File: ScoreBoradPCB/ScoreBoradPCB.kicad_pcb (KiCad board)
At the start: 2 copper layers, 100 x 100 mm, 129 parts, among them J1 Conn_01x08_Male, J10 Conn_01x02_Male, J2 Conn_01x08_Male, J3 Conn_01x08_Male, J4 Conn_01x04_Male, J5 Conn_01x04_Male, J6 Conn_01x02_Male, J7 Conn_01x02_Male, J8 Conn_01x06_Male, J9 Conn_01x02_Male, Q1 2N7002K, Q10 NP52N06SLG, Q11 2N7002K, Q12 NP52N06SLG, Q13 2N7002K, Q14 NP52N06SLG, Q15 BSS84, Q16 NP52N06SLG, Q17 2N7002K, Q18 BSS84, Q19 NP52N06SLG, Q2 NP52N06SLG, Q20 2N7002K, Q21 BSS84, Q22 NP52N06SLG, Q23 2N7002K, Q24 2N7002K, Q3 2N7002K, Q4 NP52N06SLG, Q5 2N7002K, Q6 NP52N06SLG, Q7 2N7002K, Q8 NP52N06SLG, Q9 2N7002K, SW1 SW_Push, SW2 SW_Push, SW3 SW_Push, SW4 SW_Push, SW5 SW_Push, SW6 SW_Push, SW7 SW_Push, U1 PIC16F1938, U2 TLP291, U3 IR2104, U4 TLP291, U5 IR2104, U6 TLP291, U7 IR2104

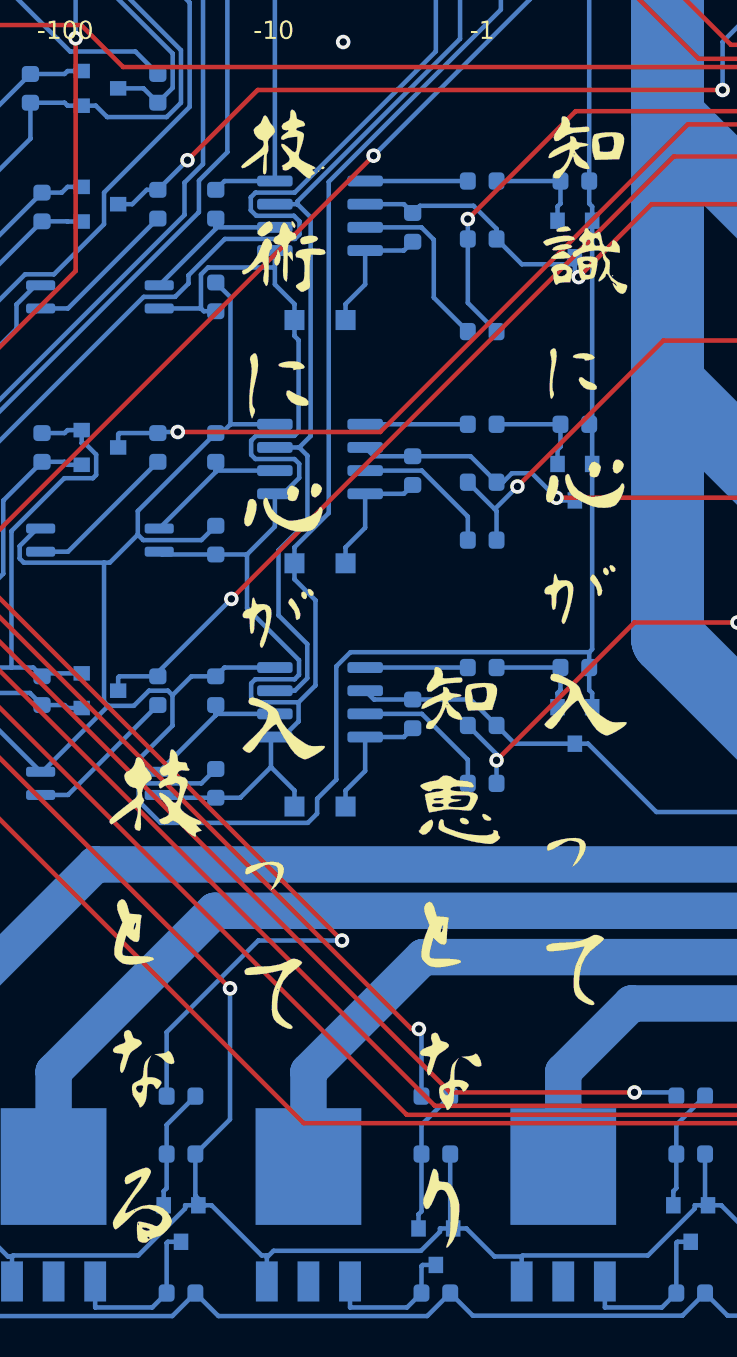
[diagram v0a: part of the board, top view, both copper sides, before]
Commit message: ゲート抵抗を削除
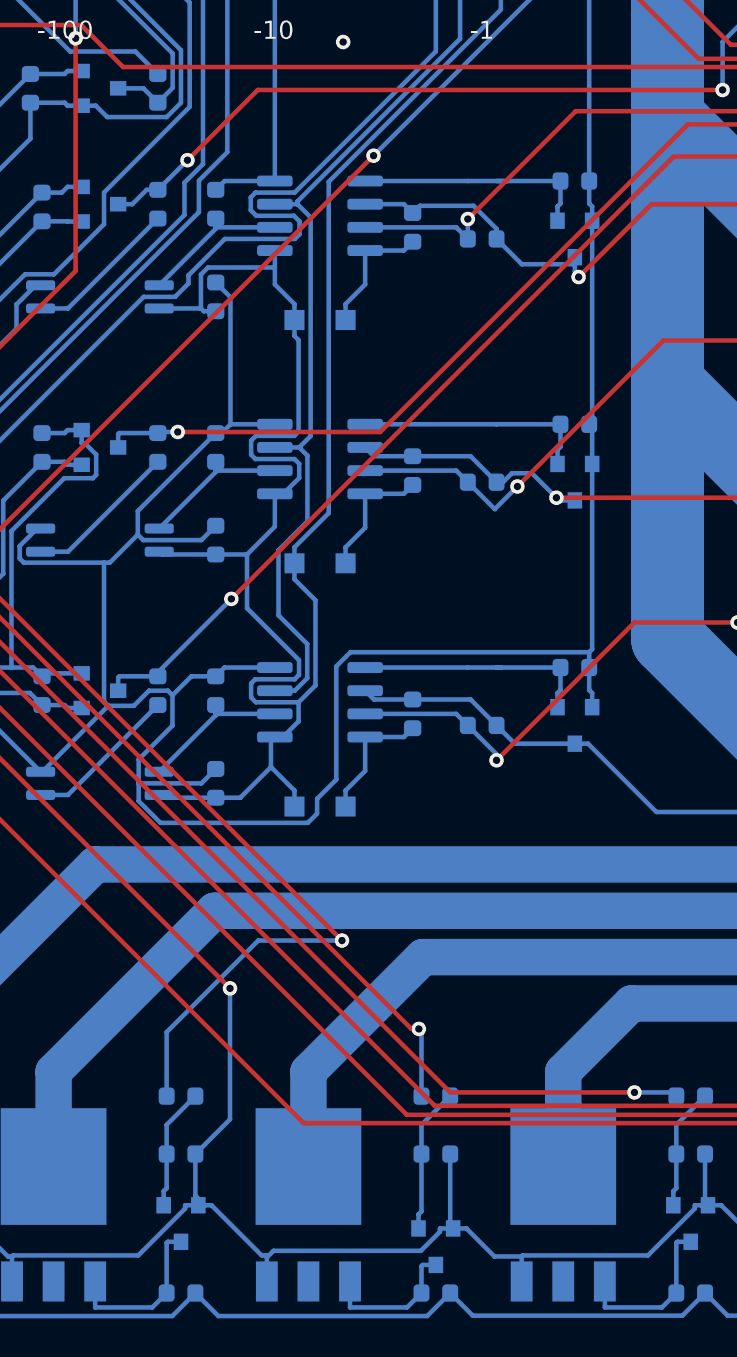
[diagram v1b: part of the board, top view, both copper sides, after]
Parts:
- removed G***: LOGO, logo:Koukun
- removed R25, R26, R32, R33, R39, R40: 100, Resistor_SMD:R_0603_1608Metric
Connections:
- U3 pad 5: Net-(R26-Pad2) -> Net-(Q17-Pad1)
- U3 pad 7: Net-(R25-Pad2) -> Net-(Q16-Pad1)
- U5 pad 5: Net-(R33-Pad2) -> Net-(Q20-Pad1)
- U5 pad 7: Net-(R32-Pad2) -> Net-(Q19-Pad1)
- U7 pad 5: Net-(R40-Pad2) -> Net-(Q23-Pad1)
- U7 pad 7: Net-(R39-Pad2) -> Net-(Q22-Pad1)
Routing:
- net Net-(R25-Pad2): track 9.85 -> 0.00 mm
- net Net-(R32-Pad2): track 7.96 -> 0.00 mm
- net Net-(R39-Pad2): track 7.96 -> 0.00 mm
- net Net-(Q17-Pad1): track 5.75 -> 13.5 mm
- net Net-(Q23-Pad1): track 5.75 -> 13.2 mm
- net Net-(Q20-Pad1): track 5.75 -> 12.9 mm
- net Net-(R40-Pad2): track 5.63 -> 0.00 mm
- net Net-(R33-Pad2): track 5.63 -> 0.00 mm
- net Net-(R26-Pad2): track 5.63 -> 0.00 mm
- net Net-(Q22-Pad1): track 23.6 -> 28.2 mm
- net Net-(Q19-Pad1): track 24.4 -> 28.5 mm

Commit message: リハーサル用
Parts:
- added G***: LOGO, logo:Koukun, F.Cu at (140.0, 110.0)
